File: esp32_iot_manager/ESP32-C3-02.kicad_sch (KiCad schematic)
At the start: 0 parts

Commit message: esp32 page and datasheets
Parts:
- added C10, C13, C14, C8: 0.1u, Capacitor_THT:C_Disc_D3.0mm_W2.0mm_P2.50mm, symbol PCM_SL_Devices:Capacitor_NP
- added C11: 1u, Capacitor_THT:C_Disc_D3.0mm_W2.0mm_P2.50mm, symbol PCM_SL_Devices:Capacitor_NP
- added C13, C7: 10u, symbol Device:C_Polarized
- added C9: 4.7u, symbol Device:C_Polarized
- added J3: GSD090012SEU, GSD090012SEU:AMPHENOL_GSD090012SEU, symbol GSD090012SEU:GSD090012SEU
- added LED5: LTST-C170GKT, LEDC2012X120N, symbol LTST-C170GKT:LTST-C170GKT
- added LED6: LTST-C170KRKT, LEDC2012X120N, symbol LTST-C170KRKT:LTST-C170KRKT
- added R11: 1K, Resistor_THT:R_Axial_DIN0207_L6.3mm_D2.5mm_P10.16mm_Horizontal, symbol PCM_SL_Resistors:Resistor
- added R12: 22.1K, symbol Device:R
- added R13: 47.5K, symbol Device:R
- added R15, R16, R20, R22: 50, Resistor_THT:R_Axial_DIN0207_L6.3mm_D2.5mm_P10.16mm_Horizontal, symbol PCM_SL_Resistors:Resistor
- added R15, R18: 470, symbol Device:R
- added R19: 10K, Resistor_THT:R_Axial_DIN0207_L6.3mm_D2.5mm_P10.16mm_Horizontal, symbol PCM_SL_Resistors:Resistor
- added U3: ESP32-C3-WROOM-02-H4, ESP32-C3-WROOM-02-H4:MODULE_ESP32-C3-WROOM-02-H4, symbol ESP32-C3-WROOM-02-H4:ESP32-C3-WROOM-02-H4
- added U4: CP2102N-Axx-xQFN20, Package_DFN_QFN:SiliconLabs_QFN-20-1EP_3x3mm_P0.5mm, symbol Interface_USB:CP2102N-Axx-xQFN20
- added U5: USBLC6-2P6, PCM_Package_TO_SOT_SMD_AKL:SOT-666, symbol PCM_Diode_TVS_AKL:USBLC6-2P6
- added U6: W25Q32JVSSIQ, W25Q32JVSSIQ:SOIC127P790X216-8N, symbol W25Q32JVSSIQ:W25Q32JVSSIQ
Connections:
- new net: R11.1, U4.9 (~{RST})
- new net: C11.2, R12.2, R13.1, U4.8 (VBUS)
- new net: R20.2, U3.5 (IO6)
- new net: LED6.1 (K), R18.1
- new net: LED5.1 (K), R15.2
- new net: R18.2, U4.19 (~{RXT}/GPIO.3)
- new net: R15.1, U4.20 (~{TXT}/GPIO.2)
- new net: R15.1, U3.6 (IO7)
- new net: J3.7 (DAT0), R16.2
- new net: C14.2, U6.8 (VCC)
- new net: R22.1, U6.2 (DO(IO1))
- new net 3.3V: C10.1, C13.1, C13.2, C7.1, C8.2, C9.1, J3.4 (VDD1), LED5.2 (A), LED6.2 (A), R11.2, R19.1, U3.1 (3V3), U4.6 (VDD), U4.7 (VREGIN), U6.3 (~{WP}(IO2)), U6.7 (~{HOLD}/~{RESET}(IO3))
- new net BOOT: U3.8 (IO9)
- new net CS: U3.10 (IO10), U6.1 (~{CS})
- new net CS_SD: J3.1 (CD/DAT3), R19.2, U3.18 (IO0)
- new net DTS: U4.15 (~{CTS})
- new net EN: U3.2 (EN)
- new net GND: C10.2, C11.1, C13.1, C13.2, C14.1, C7.2, C8.1, C9.2, J3.3 (VSS1), J3.6 (VSS2), J3.8 (DAT1), J3.9 (DAT2), J3.G1 (SHIELD_GND), J3.G2 (SHIELD_GND), J3.G3 (SHIELD_GND), J3.G4 (SHIELD_GND), R13.2, U3.19 (GND), U3.20 (GND), U3.21 (GND), U3.22 (GND), U3.23 (GND), U3.24 (GND), U3.25 (GND), U3.26 (GND), U3.27 (GND), U3.28 (GND), U3.29 (GND), U3.30 (GND), U3.31 (GND), U3.32 (GND), U3.33 (GND), U3.34 (GND), U3.35 (GND), U3.36 (GND), U3.37 (GND), U3.38 (GND), U3.39 (GND), U3.9 (GND), U4.12 (GND), U4.21 (GND), U4.3 (GND), U5.2 (VN), U6.4 (GND)
- new net GPI019: U3.14 (IO19)
- new net GPIO18: U3.13 (IO18)
- new net GPIO8: U3.7 (IO8)
- new net MIC_OUT: U3.4 (IO5)
- new net MISO_DO: R16.1, R22.2, U3.16 (IO2)
- new net MOSI_DI: J3.2 (CMD), R15.2, U6.5 (DI(IO0))
- new net PHOTO_C: U3.17 (IO1)
- new net RTS: U4.16 (~{RTS})
- new net RX_TX: U3.11 (RXD), U4.17 (RXD)
- new net SCL: U3.15 (IO3)
- new net SCLK: J3.5 (CLK), R20.1, U6.6 (CLK)
- new net SDA: U3.3 (IO4)
- new net TX_RX: U3.12 (TXD), U4.18 (TXD)
- new net USB_DATA+: U4.4 (D+), U5.3 (L2)
- new net USB_DATA-: U4.5 (D-), U5.1 (L1)
- new net USB_DN: U5.6 (L1)
- new net USB_DP: U5.4 (L2)
- new net V_BUS: R12.1, U5.5 (VP)
- no-connect marks 0 -> 7
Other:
- note added: "ESP32"
- note added: "Flash Memory"
- note added: "SD Card"
- note added: "USB Module"

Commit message: finished esp32 sheet, next sensors
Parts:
- added TP1: Test MOSI, symbol Connector:TestPoint
- added TP2: Test MISO, symbol Connector:TestPoint
- added TP3: Test clock, symbol Connector:TestPoint
- added TP4: Test CS, symbol Connector:TestPoint
- added TP5: Test CS_SD, symbol Connector:TestPoint
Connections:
- net 3.3V: now also C13.1; no longer C13.2
- net CS: now also TP4.1
- net CS_SD: now also TP5.1
- net GND: now also C13.2; no longer C13.1
- net MISO_DO: now also TP2.1
- net MOSI_DI: now also TP1.1
- net SCLK: now also TP3.1
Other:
- added sheet Sensors (sensors.kicad_sch)
- added sheet User Interface (user_interface.kicad_sch)
- note added: "Test points"
- title: (none) -> ESP32 C3 USB and Flash memory SD card
- moved on the sheet: C13, C14, J3, R16, R19, R22, U6

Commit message: sensor and user interface done
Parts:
- C10, C11, C8: footprint Capacitor_THT:C_Disc_D3.0mm_W2.0mm_P2.50mm -> Capacitor_SMD:C_0805_2012Metric
- C13, C7, C9: footprint (none) -> esp32_manager_project:T491A
- C14: renamed from C13; footprint Capacitor_THT:C_Disc_D3.0mm_W2.0mm_P2.50mm -> Capacitor_SMD:C_0805_2012Metric
- C15: renamed from C14; footprint Capacitor_THT:C_Disc_D3.0mm_W2.0mm_P2.50mm -> Capacitor_SMD:C_0805_2012Metric
- LED5, LED6: footprint LEDC2012X120N -> esp32_manager_project:LEDC2012X120N
- R11, R15, R19, R20, R22: footprint Resistor_THT:R_Axial_DIN0207_L6.3mm_D2.5mm_P10.16mm_Horizontal -> Resistor_SMD:R_0805_2012Metric
- R12, R13, R18: footprint (none) -> Resistor_SMD:R_0805_2012Metric
- R16: renamed from R15; footprint (none) -> Resistor_SMD:R_0805_2012Metric
- R17: renamed from R16; footprint Resistor_THT:R_Axial_DIN0207_L6.3mm_D2.5mm_P10.16mm_Horizontal -> Resistor_SMD:R_0805_2012Metric
- TP1, TP2, TP3, TP4, TP5: footprint (none) -> TestPoint:TestPoint_Pad_D1.0mm
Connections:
- net DTS renamed DTR
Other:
- sheet Sensors ports: added MIC_OUT, PHOTO_C, SCL, SDA; removed none
- sheet User Interface ports: added BOOT, DTR, EN, GPIO18, GPIO19, GPIO8, RTS, SCL, SDA; removed none

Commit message: finished design of pcb, next copper zones, routing
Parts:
- J3: footprint GSD090012SEU:AMPHENOL_GSD090012SEU -> esp32_manager_project:AMPHENOL_GSD090012SEU
- U3: footprint ESP32-C3-WROOM-02-H4:MODULE_ESP32-C3-WROOM-02-H4 -> esp32_manager_project:MODULE_ESP32-C3-WROOM-02-H4
- U4: footprint Package_DFN_QFN:SiliconLabs_QFN-20-1EP_3x3mm_P0.5mm -> PCM_Package_DFN_QFN_AKL:SiliconLabs_QFN-20-1EP_3x3mm_P0.5mm
- U6: footprint W25Q32JVSSIQ:SOIC127P790X216-8N -> esp32_manager_project:SOIC127P790X216-8N
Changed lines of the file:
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@@
 			)
 		)
-		(property "Footprint" "Package_DFN_QFN:SiliconLabs_QFN-20-1EP_3x3mm_P0.5mm"
+		(property "Footprint" "PCM_Package_DFN_QFN_AKL:SiliconLabs_QFN-20-1EP_3x3mm_P0.5mm"
 			(at 101.6 172.72 0)
 			(effects
@@
 			)
 		)
-		(property "Footprint" "ESP32-C3-WROOM-02-H4:MODULE_ESP32-C3-WROOM-02-H4"
+		(property "Footprint" "esp32_manager_project:MODULE_ESP32-C3-WROOM-02-H4"
 			(at 226.06 48.26 0)
 			(effects
@@
 			)
 		)
-		(property "Footprint" "GSD090012SEU:AMPHENOL_GSD090012SEU"
+		(property "Footprint" "esp32_manager_project:AMPHENOL_GSD090012SEU"
 			(at 219.71 97.79 0)
 			(effects
@@
 			)
 		)
-		(property "Footprint" "W25Q32JVSSIQ:SOIC127P790X216-8N"
+		(property "Footprint" "esp32_manager_project:SOIC127P790X216-8N"
 			(at 63.5 36.83 0)
 			(effects

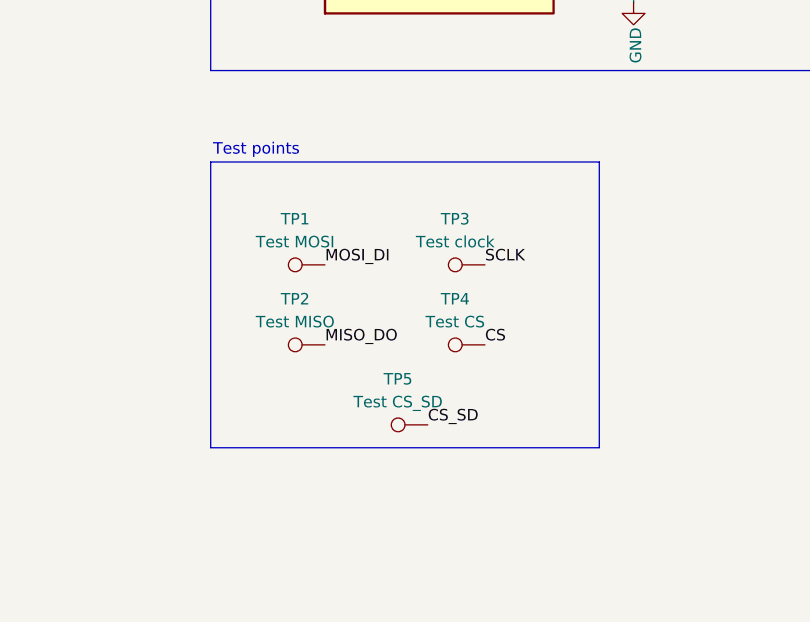
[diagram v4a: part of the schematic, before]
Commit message: added 3.3v testpoint, routed diff pairs
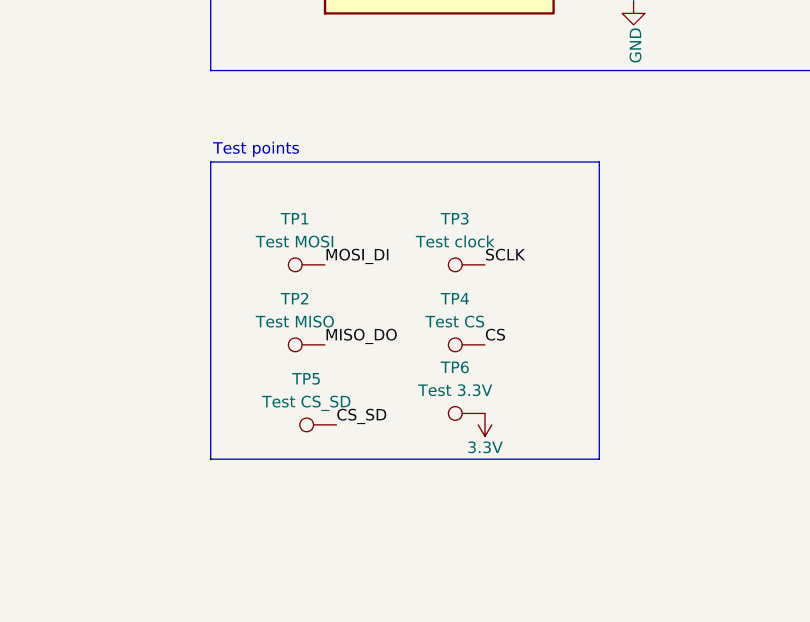
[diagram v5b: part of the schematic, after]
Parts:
- added TP6: Test 3.3V, TestPoint:TestPoint_Pad_D1.0mm, symbol Connector:TestPoint
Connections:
- net 3.3V: now also TP6.1
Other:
- moved on the sheet: TP5
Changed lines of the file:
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@@
 	(rectangle
 		(start 194.31 129.54)
-		(end 237.49 161.29)
+		(end 237.49 162.56)
 		(stroke
 			(width 0)
@@
 	)
 	(label "CS_SD"
-		(at 218.44 158.75 0)
+		(at 208.28 158.75 0)
 		(effects
 			(font
@@
 	)
 	(symbol
+		(lib_id "PCM_SparkFun-PowerSymbol:3.3V")
+		(at 224.79 157.48 180)
+		(unit 1)
+		(exclude_from_sim no)
+		(in_bom yes)
+		(on_board yes)
+		(dnp no)
+		(fields_autoplaced yes)
+		(property "Reference" "#PWR09"
+			(at 224.79 153.67 0)
+			(effects
+				(font
+					(size 1.27 1.27)
+				)
+				(hide yes)
+			)
+		)
+		(property "Value" "3.3V"
+			(at 224.79 161.29 0)
+			(do_not_autoplace yes)
+			(effects
+				(font
+					(size 1.27 1.27)
+				)
+			)
+		)
+		(property "Footprint" ""
+			(at 224.79 157.48 0)
+			(effects
+				(font
+					(size 1.27 1.27)
+				)
+				(hide yes)
+			)
+		)
+		(property "Datasheet" ""
+			(at 224.79 157.48 0)
+			(effects
+				(font
+					(size 1.27 1.27)
+				)
+				(hide yes)
+			)
+		)
+		(property "Description" "Power symbol creates a global label with name \"3.3V\""
+			(at 224.79 151.13 0)
+			(effects
+				(font
+					(size 1.27 1.27)
+				)
+				(hide yes)
+			)
+		)
+		(pin "1"
+		)
+		(instances
+			(project "esp32_iot_manager"
+				(path "/6166e74a-1734-44f8-8d71-dfcab5cab94e/1ee81c10-782d-4aea-8ae0-4dace1450d31"
+					(reference "#PWR09")
+					(unit 1)
+				)
+			)
+		)
+	)
+	(symbol
 		(lib_id "LTST-C170KRKT:LTST-C170KRKT")
 		(at 119.38 161.29 0)
@@
 	)
 	(symbol
+		(lib_id "Connector:TestPoint")
+		(at 224.79 157.48 90)
+		(unit 1)
+		(exclude_from_sim no)
+		(in_bom yes)
+		(on_board yes)
+		(dnp no)
+		(fields_autoplaced yes)
+		(property "Reference" "TP6"
+			(at 221.488 152.4 90)
+			(effects
+				(font
+					(size 1.27 1.27)
+				)
+			)
+		)
+		(property "Value" "Test 3.3V"
+			(at 221.488 154.94 90)
+			(effects
+				(font
+					(size 1.27 1.27)
+				)
+			)
+		)
+		(property "Footprint" "TestPoint:TestPoint_Pad_D1.0mm"
+			(at 224.79 152.4 0)
+			(effects
+				(font
+					(size 1.27 1.27)
+				)
+				(hide yes)
+			)
+		)
+		(property "Datasheet" "~"
+			(at 224.79 152.4 0)
+			(effects
+				(font
+					(size 1.27 1.27)
+				)
+				(hide yes)
+			)
+		)
+		(property "Description" "test point"
+			(at 224.79 157.48 0)
+			(effects
+				(font
+					(size 1.27 1.27)
+				)
+				(hide yes)
+			)
+		)
+		(pin "1"
+		)
+		(instances
+			(project ""
+				(path "/6166e74a-1734-44f8-8d71-dfcab5cab94e/1ee81c10-782d-4aea-8ae0-4dace1450d31"
+					(reference "TP6")
+					(unit 1)
+				)
+			)
+		)
+	)
+	(symbol
 		(lib_id "PCM_SparkFun-PowerSymbol:3.3V")
 		(at 248.92 101.6 270)
@@
 	(symbol
 		(lib_id "Connector:TestPoint")
-		(at 218.44 158.75 90)
+		(at 208.28 158.75 90)
 		(unit 1)
 		(exclude_from_sim no)
@@
 		(fields_autoplaced yes)
 		(property "Reference" "TP5"
-			(at 215.138 153.67 90)
+			(at 204.978 153.67 90)
 			(effects
 				(font
@@
 		)
 		(property "Value" "Test CS_SD"
-			(at 215.138 156.21 90)
+			(at 204.978 156.21 90)
 			(effects
 				(font
@@
 		)
 		(property "Footprint" "TestPoint:TestPoint_Pad_D1.0mm"
-			(at 218.44 153.67 0)
+			(at 208.28 153.67 0)
 			(effects
 				(font
@@
 		)
 		(property "Datasheet" "~"
-			(at 218.44 153.67 0)
+			(at 208.28 153.67 0)
 			(effects
 				(font
@@
 		)
 		(property "Description" "test point"
-			(at 218.44 158.75 0)
+			(at 208.28 158.75 0)
 			(effects
 				(font

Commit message: FIX DRC
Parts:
- added TP7: Test 5V, TestPoint:TestPoint_Pad_D1.0mm, symbol Connector:TestPoint
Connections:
- new net +5V: TP7.1
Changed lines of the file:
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@@
 	(rectangle
 		(start 194.31 129.54)
-		(end 237.49 162.56)
+		(end 252.73 162.56)
 		(stroke
 			(width 0)
@@
 	)
 	(symbol
+		(lib_id "Connector:TestPoint")
+		(at 241.3 140.97 90)
+		(unit 1)
+		(exclude_from_sim no)
+		(in_bom yes)
+		(on_board yes)
+		(dnp no)
+		(fields_autoplaced yes)
+		(property "Reference" "TP7"
+			(at 237.998 135.89 90)
+			(effects
+				(font
+					(size 1.27 1.27)
+				)
+			)
+		)
+		(property "Value" "Test 5V"
+			(at 237.998 138.43 90)
+			(effects
+				(font
+					(size 1.27 1.27)
+				)
+			)
+		)
+		(property "Footprint" "TestPoint:TestPoint_Pad_D1.0mm"
+			(at 241.3 135.89 0)
+			(effects
+				(font
+					(size 1.27 1.27)
+				)
+				(hide yes)
+			)
+		)
+		(property "Datasheet" "~"
+			(at 241.3 135.89 0)
+			(effects
+				(font
+					(size 1.27 1.27)
+				)
+				(hide yes)
+			)
+		)
+		(property "Description" "test point"
+			(at 241.3 140.97 0)
+			(effects
+				(font
+					(size 1.27 1.27)
+				)
+				(hide yes)
+			)
+		)
+		(pin "1"
+		)
+		(instances
+			(project "esp32_iot_manager"
+				(path "/6166e74a-1734-44f8-8d71-dfcab5cab94e/1ee81c10-782d-4aea-8ae0-4dace1450d31"
+					(reference "TP7")
+					(unit 1)
+				)
+			)
+		)
+	)
+	(symbol
 		(lib_id "LTST-C170KRKT:LTST-C170KRKT")
 		(at 119.38 161.29 0)
@@
 					(unit 1)
 				)
+			)
+		)
+	)
+	(symbol
+		(lib_id "power:+5V")
+		(at 241.3 140.97 270)
+		(unit 1)
+		(exclude_from_sim no)
+		(in_bom yes)
+		(on_board yes)
+		(dnp no)
+		(fields_autoplaced yes)
+		(property "Reference" "#PWR056"
+			(at 237.49 140.97 0)
+			(effects
+				(font
+					(size 1.27 1.27)
+				)
+				(hide yes)
+			)
+		)
+		(property "Value" "+5V"
+			(at 245.11 140.9699 90)
+			(effects
+				(font
+					(size 1.27 1.27)
+				)
+				(justify left)
+			)
+		)
+		(property "Footprint" ""
+			(at 241.3 140.97 0)
+			(effects
+				(font
+					(size 1.27 1.27)
+				)
+				(hide yes)
+			)
+		)
+		(property "Datasheet" ""
+			(at 241.3 140.97 0)
+			(effects
+				(font
+					(size 1.27 1.27)
+				)
+				(hide yes)
+			)
+		)
+		(property "Description" "Power symbol creates a global label with name \"+5V\""
+			(at 241.3 140.97 0)
+			(effects
+				(font
+					(size 1.27 1.27)
+				)
+				(hide yes)
+			)
+		)
+		(pin "1"
+		)
+		(instances
+			(project ""
+				(path "/6166e74a-1734-44f8-8d71-dfcab5cab94e/1ee81c10-782d-4aea-8ae0-4dace1450d31"
+					(reference "#PWR056")
+					(unit 1)
+				)
